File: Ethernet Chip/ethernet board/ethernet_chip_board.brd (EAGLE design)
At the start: 110.4 x 78 mm, 24 parts, among them Q1 ASV-8

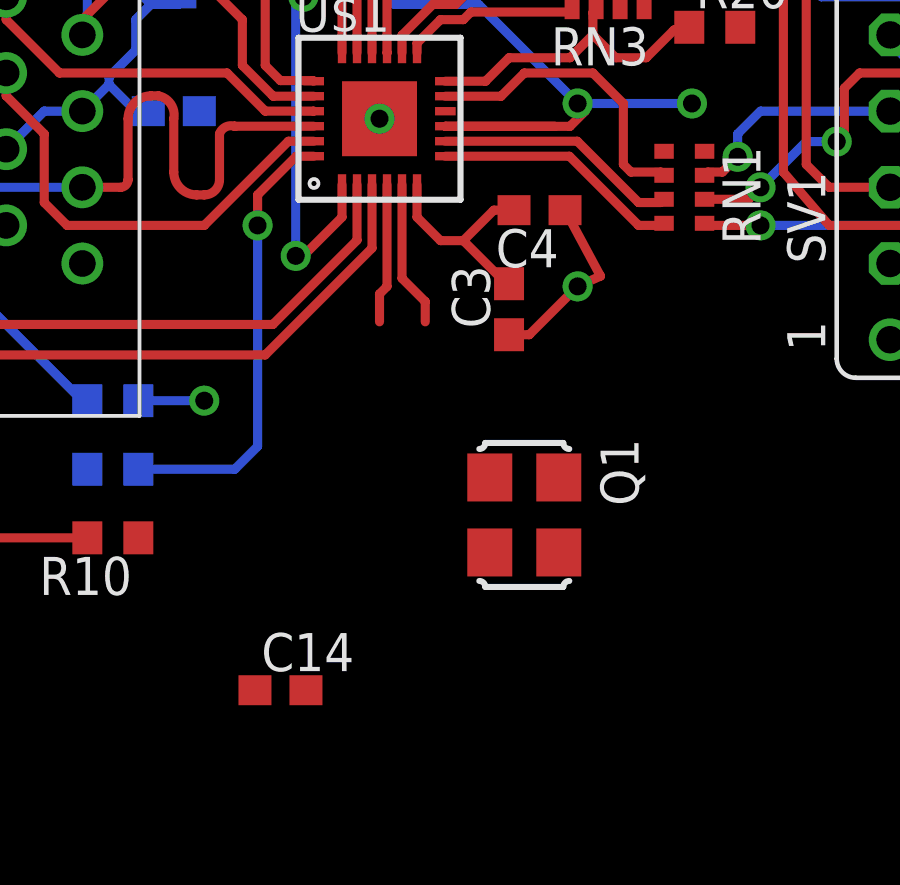
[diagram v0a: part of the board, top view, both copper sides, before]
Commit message: "Added 50 MHz Oscillator"
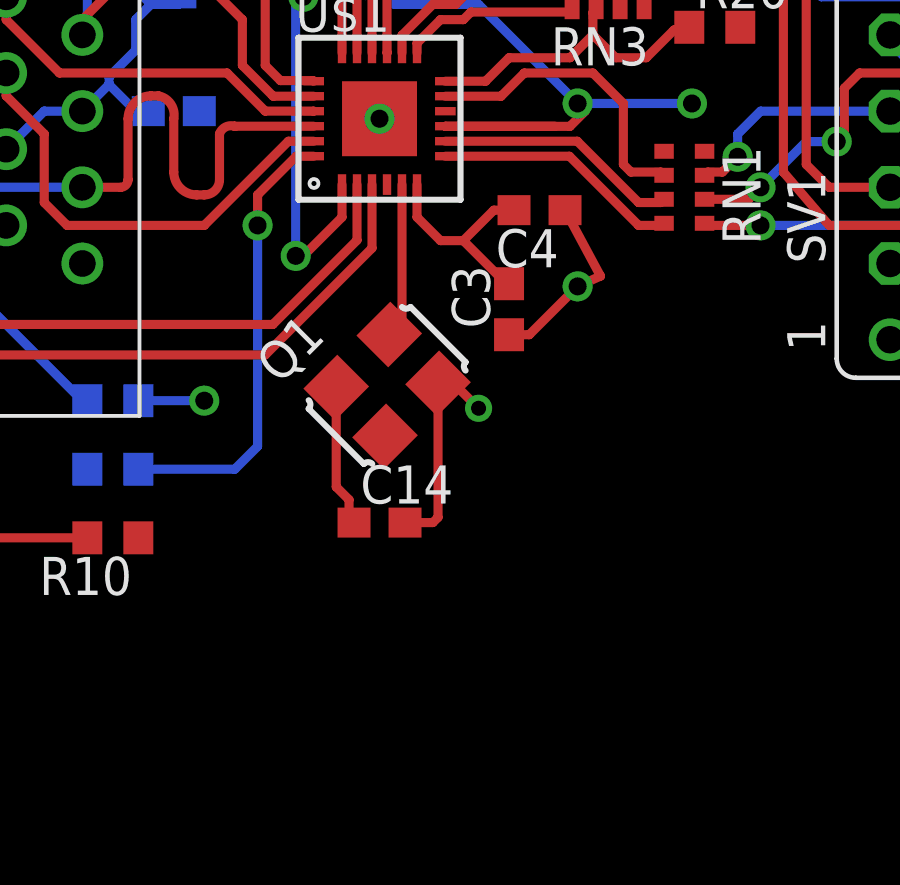
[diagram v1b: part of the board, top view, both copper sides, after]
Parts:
- moved C14 6.49 mm to (27.7, 32.0)
- moved Q1 6.29 mm to (27.9, 36.6), turned to 45 degrees
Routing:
- net GND: track 10.2 -> 17.5 mm, vias 4 -> 5
- net +3V3: track 69.3 -> 74.0 mm
- net XTAL2: track 4.68 -> 0.00 mm
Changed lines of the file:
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@@
 <attribute name="MPN" value="" x="35.306" y="49.784" size="1.778" layer="27" display="off"/>
 </element>
-<element name="Q1" library="MicroBoard" package="ASF" value="ASV-8" x="32.512" y="32.258" rot="R270">
-<attribute name="DIGIKEY" value="535-10066-1-ND" x="41.148" y="40.386" size="1.778" layer="27" rot="R270" display="off"/>
+<element name="Q1" library="MicroBoard" package="ASF" value="ASV-8" x="27.94" y="36.576" rot="R45">
+<attribute name="DIGIKEY" value="535-10066-1-ND" x="16.086059375" y="36.935209375" size="1.778" layer="27" rot="R45" display="off"/>
 </element>
-<element name="C14" library="resistor" package="C0603" value="0.01uF" x="24.384" y="26.416"/>
+<element name="C14" library="resistor" package="C0603" value="0.01uF" x="27.686" y="32.004"/>
 </elements>
 <signals>
@@
 <contactref element="Q1" pad="2"/>
 <contactref element="C14" pad="2"/>
-<wire x1="44.704" y1="40.64" x2="47.244" y2="40.64" width="0" layer="19" extent="1-1"/>
-<wire x1="35.052" y1="40.22" x2="44.704" y2="40.64" width="0" layer="19" extent="1-1"/>
-<wire x1="27.686" y1="45.466" x2="33.87" y2="42.418" width="0" layer="19" extent="1-1"/>
-<wire x1="21.678" y1="45.72" x2="27.686" y2="45.466" width="0" layer="19" extent="1-16"/>
-<wire x1="21.082" y1="51.396" x2="21.678" y2="45.72" width="0" layer="19" extent="16-16"/>
-<wire x1="17.78" y1="40.64" x2="21.678" y2="45.72" width="0" layer="19" extent="16-16"/>
-<wire x1="11.938" y1="37.211" x2="17.78" y2="40.64" width="0" layer="19" extent="1-1"/>
-<wire x1="17.946" y1="33.782" x2="17.78" y2="40.64" width="0" layer="19" extent="16-16"/>
-<wire x1="23.456" y1="57.912" x2="21.082" y2="51.396" width="0" layer="19" extent="1-16"/>
-<wire x1="11.938" y1="52.959" x2="21.082" y2="51.396" width="0" layer="19" extent="16-16"/>
-<wire x1="11.684" y1="56.388" x2="11.938" y2="52.959" width="0" layer="19" extent="1-1"/>
-<wire x1="31.362" y1="31.008" x2="17.946" y2="33.782" width="0" layer="19" extent="1-16"/>
-<wire x1="25.234" y1="26.416" x2="31.362" y2="31.008" width="0" layer="19" extent="1-1"/>
+<wire x1="29.63705625" y1="36.646709375" x2="29.63705625" y2="32.17705625" width="0.3048" layer="1"/>
+<wire x1="29.63705625" y1="32.17705625" x2="29.464" y2="32.004" width="0.3048" layer="1"/>
+<wire x1="29.464" y1="32.004" x2="28.536" y2="32.004" width="0.3048" layer="1"/>
+<via x="30.988" y="35.814" extent="1-16" drill="0.5"/>
+<wire x1="29.63705625" y1="36.646709375" x2="30.155290625" y2="36.646709375" width="0.3048" layer="1"/>
+<wire x1="30.155290625" y1="36.646709375" x2="30.988" y2="35.814" width="0.3048" layer="1"/>
 </signal>
 <signal name="+3V3">
@@
 <contactref element="Q1" pad="4"/>
 <contactref element="C14" pad="1"/>
-<wire x1="38.1" y1="45.974" x2="39.712" y2="48.514" width="0" layer="19" extent="1-1"/>
-<wire x1="19.646" y1="36.068" x2="15.24" y2="44.45" width="0" layer="19" extent="16-16"/>
-<wire x1="19.646" y1="31.496" x2="19.646" y2="36.068" width="0" layer="19" extent="1-16"/>
-<wire x1="44.704" y1="38.1" x2="38.1" y2="45.974" width="0" layer="19" extent="1-1"/>
-<wire x1="47.244" y1="38.1" x2="44.704" y2="38.1" width="0" layer="19" extent="1-1"/>
-<wire x1="33.662" y1="33.508" x2="19.646" y2="31.496" width="0" layer="19" extent="1-1"/>
-<wire x1="23.534" y1="26.416" x2="33.662" y2="33.508" width="0" layer="19" extent="1-1"/>
+<wire x1="26.242940625" y1="36.5052875" x2="26.242940625" y2="33.193059375" width="0.3048" layer="1"/>
+<wire x1="26.242940625" y1="33.193059375" x2="26.67" y2="32.766" width="0.3048" layer="1"/>
+<wire x1="26.67" y1="32.766" x2="26.67" y2="32.17" width="0.3048" layer="1"/>
+<wire x1="26.67" y1="32.17" x2="26.836" y2="32.004" width="0.3048" layer="1"/>
 </signal>
 <signal name="N$5">
@@
 <signal name="XTAL2">
 <contactref element="U$1" pad="4"/>
-<wire x1="27.936" y1="43.271" x2="27.936" y2="39.874" width="0.3048" layer="1"/>
-<wire x1="27.936" y1="39.874" x2="27.686" y2="39.624" width="0.3048" layer="1"/>
-<wire x1="27.686" y1="39.624" x2="27.686" y2="38.696" width="0.3048" layer="1"/>
 </signal>
 <signal name="XTAL1">
 <contactref element="U$1" pad="5"/>
-<wire x1="28.436" y1="43.271" x2="28.436" y2="40.144" width="0.3048" layer="1"/>
-<wire x1="28.436" y1="40.144" x2="29.21" y2="39.37" width="0.3048" layer="1"/>
-<wire x1="29.21" y1="39.37" x2="29.21" y2="38.696" width="0.3048" layer="1"/>
 <contactref element="Q1" pad="3"/>
-<wire x1="33.662" y1="31.008" x2="29.21" y2="38.696" width="0" layer="19" extent="1-1"/>
+<wire x1="28.436" y1="43.271" x2="28.436" y2="38.698346875" width="0.3048" layer="1"/>
+<wire x1="28.436" y1="38.698346875" x2="28.010709375" y2="38.27305625" width="0.3048" layer="1"/>
 </signal>
 <signal name="MDC">
